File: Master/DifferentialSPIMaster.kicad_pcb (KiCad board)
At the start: 4 copper layers, 55.9 x 61 mm, 37 parts, among them J1 Motor Encoder 0, J2 Conn_01x20, J3 Motor Encoder 0, U1 MAX485E, U2 MAX485E, U3 MAX485E, U4 MAX485E, U5 MAX485E, U6 MAX485E

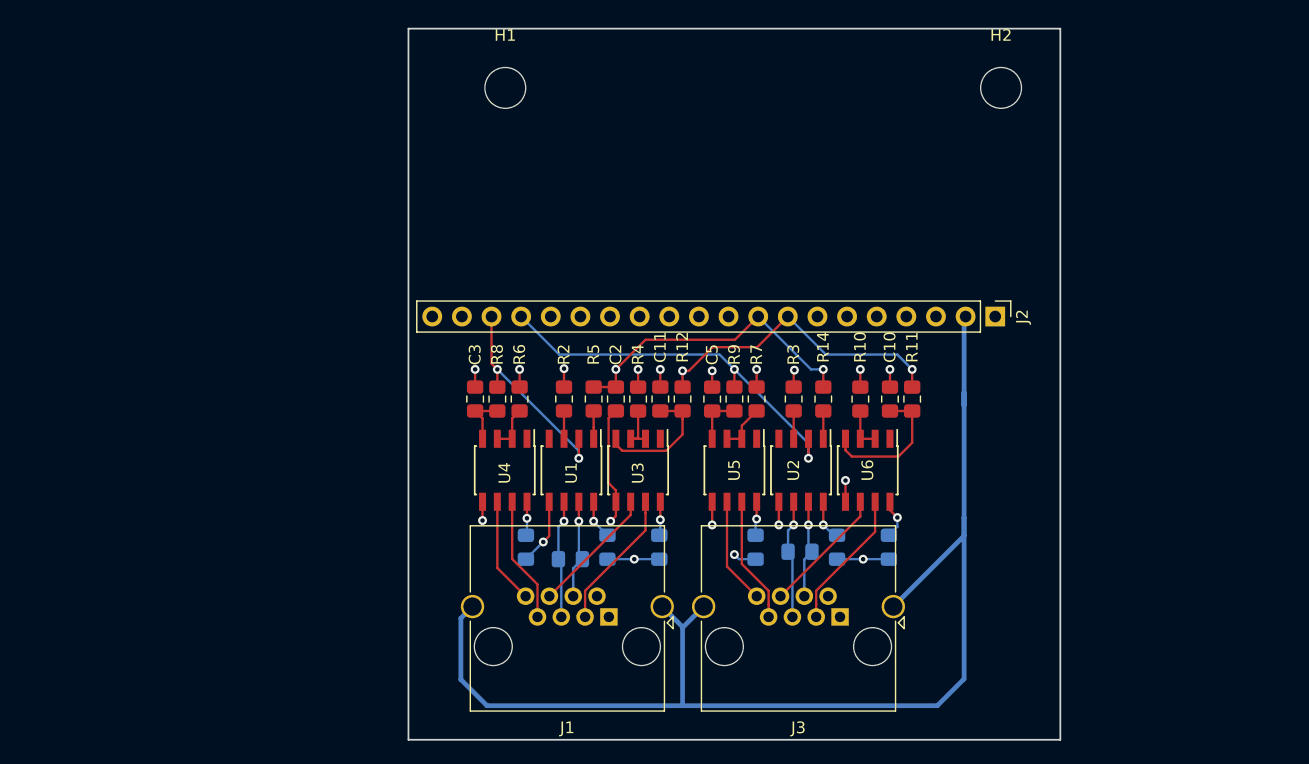
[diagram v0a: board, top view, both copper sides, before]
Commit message: Move board edge closer to RJ45s
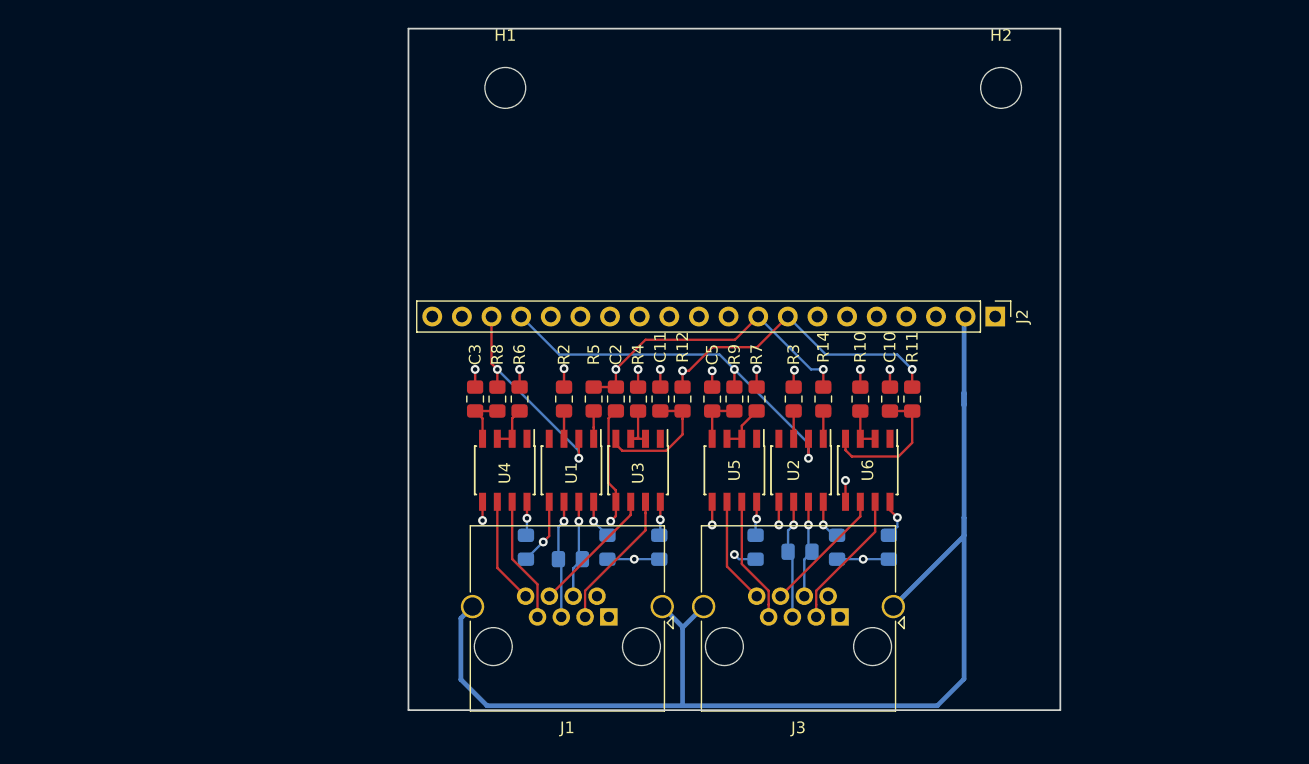
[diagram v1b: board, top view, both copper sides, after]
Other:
- board size 55.9 x 61 mm -> 55.9 x 58.4 mm
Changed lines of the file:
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@@
     )
   )
-  (gr_line (start 149.725 125.815) (end 93.845 125.815) (layer Edge.Cuts) (width 0.15))
-  (gr_line (start 149.725 64.855) (end 149.725 125.815) (layer Edge.Cuts) (width 0.15))
+  (gr_line (start 149.725 123.275) (end 93.845 123.275) (layer Edge.Cuts) (width 0.15))
+  (gr_line (start 149.725 64.855) (end 149.725 123.275) (layer Edge.Cuts) (width 0.15))
   (gr_line (start 93.845 64.855) (end 149.725 64.855) (layer Edge.Cuts) (width 0.15))
-  (gr_line (start 93.845 125.815) (end 93.845 64.855) (layer Edge.Cuts) (width 0.15))
+  (gr_line (start 93.845 123.275) (end 93.845 64.855) (layer Edge.Cuts) (width 0.15))
   (via (at 105.402 108.8605) (size 0.762) (drill 0.381) (layers F.Cu B.Cu) (net 1))
   (segment (start 103.915 110.335) (end 105.3895 108.8605) (width 0.2032) (layer B.Cu) (net 1))
@@
     (polygon
       (pts
-        (xy 93.845 87.715) (xy 149.725 87.715) (xy 149.725 125.815) (xy 93.845 125.815)
+        (xy 93.845 87.715) (xy 149.725 87.715) (xy 149.725 123.275) (xy 93.845 123.275)
       )
     )
@@
     (polygon
       (pts
-        (xy 93.845 87.715) (xy 149.725 87.715) (xy 149.725 125.815) (xy 93.845 125.815)
+        (xy 93.845 87.715) (xy 149.725 87.715) (xy 149.725 123.275) (xy 93.845 123.275)
       )
     )

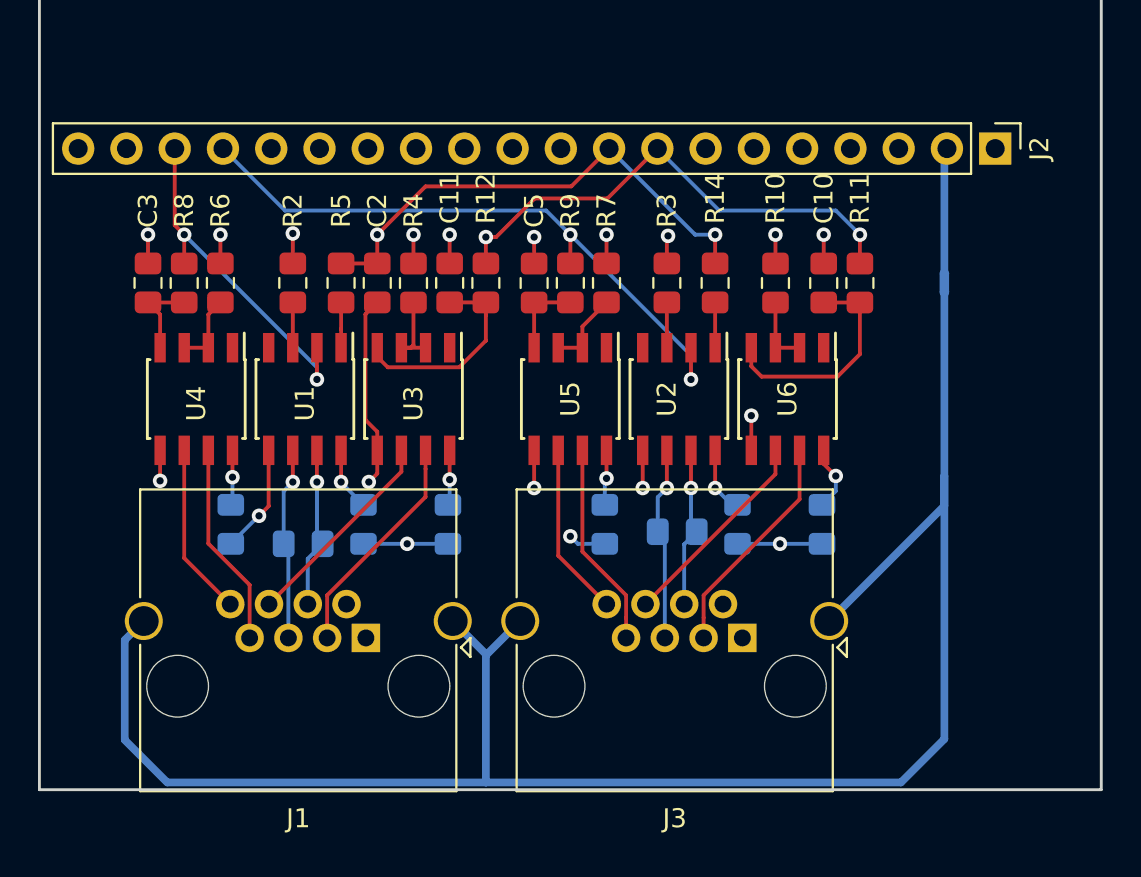
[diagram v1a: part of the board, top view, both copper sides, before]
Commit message: Add top/bottom fills, make board 2 layer
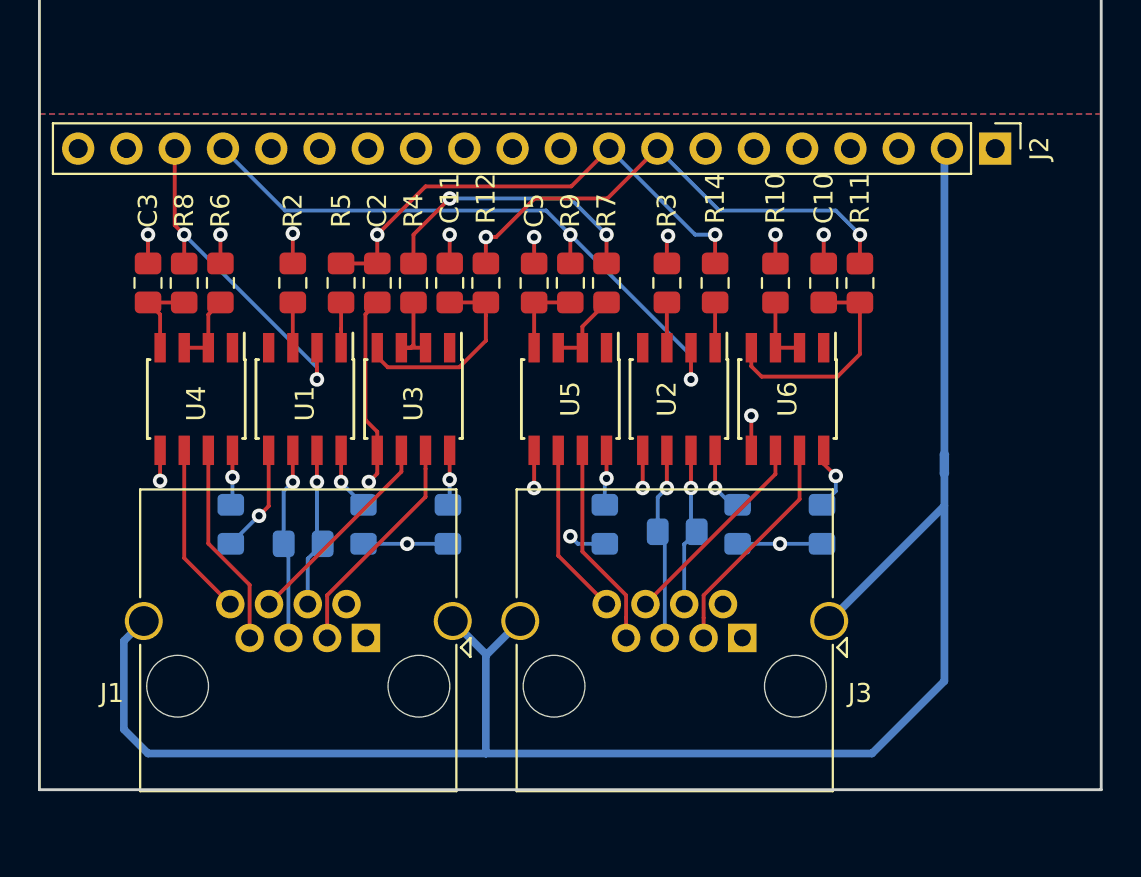
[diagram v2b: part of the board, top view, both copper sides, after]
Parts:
- moved NT1 9.52 mm to (141.5, 106.1)
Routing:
- net GND: track 97.1 -> 81.2 mm
- net +5V: track 25.1 -> 36.9 mm
- net GNDD: track 49.8 -> 59.3 mm
- added copper zone on F.Cu, net +5V
- added copper zone on B.Cu, net GNDD
- removed copper zone on In2.Cu, net +5V
- removed copper zone on In1.Cu, net GNDD
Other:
- copper layers 4 -> 2
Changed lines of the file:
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@@
     (thickness 1.6)
     (drawings 4)
-    (tracks 213)
+    (tracks 215)
     (zones 0)
     (modules 37)
@@
   (layers
     (0 F.Cu signal)
-    (1 In1.Cu signal)
-    (2 In2.Cu signal)
     (31 B.Cu signal)
     (32 B.Adhes user)
@@
     (46 B.CrtYd user)
     (47 F.CrtYd user)
-    (48 B.Fab user hide)
-    (49 F.Fab user hide)
+    (48 B.Fab user)
+    (49 F.Fab user)
   )
   (setup
@@
   )
   (module NetTie:NetTie-2_SMD_Pad0.5mm (layer B.Cu)
-    (at 141.47 96.605 90)
+    (at 141.47 106.13 90)
     (descr "Net tie, 2 pin, 0.5mm square SMD pads")
     (tags "net tie")
@@
     (descr "Shielded, https://www.amphenolcanada.com/ProductSearch/drawings/AC/RJHSE538X.pdf")
     (tags "RJ45 8p8c ethernet cat5")
-    (fp_text reference J3 (at 3.56 -9.5 180) (layer F.SilkS)
+    (fp_text reference J3 (at -6.186 -2.907 180) (layer F.SilkS)
       (effects (font (size 1 1) (thickness 0.15)))
     )
@@
     (descr "Shielded, https://www.amphenolcanada.com/ProductSearch/drawings/AC/RJHSE538X.pdf")
     (tags "RJ45 8p8c ethernet cat5")
-    (fp_text reference J1 (at 3.56 -9.5 180) (layer F.SilkS)
+    (fp_text reference J1 (at 13.372 -2.907 180) (layer F.SilkS)
       (effects (font (size 1 1) (thickness 0.15)))
     )
@@
   (segment (start 135.12 95.585) (end 135.12 94.065) (width 0.2032) (layer F.Cu) (net 1))
   (segment (start 141.47 89.67) (end 141.605 89.535) (width 0.4064) (layer B.Cu) (net 1))
-  (segment (start 141.47 96.105) (end 141.47 89.67) (width 0.4064) (layer B.Cu) (net 1))
+  (segment (start 141.47 105.63) (end 141.47 89.67) (width 0.4064) (layer B.Cu) (net 1))
   (segment (start 114.165 106.3932) (end 114.165 105.415) (width 0.2032) (layer F.Cu) (net 2))
   (segment (start 114.165 107.864078) (end 114.165 106.3932) (width 0.2032) (layer F.Cu) (net 2))
@@
   (segment (start 101.465 111.086) (end 103.887 113.508) (width 0.2032) (layer F.Cu) (net 7))
   (segment (start 101.465 105.415) (end 101.465 111.086) (width 0.2032) (layer F.Cu) (net 7))
-  (segment (start 98.337001 115.397999) (end 98.337001 120.655001) (width 0.4064) (layer B.Cu) (net 8))
-  (segment (start 99.337 114.398) (end 98.337001 115.397999) (width 0.4064) (layer B.Cu) (net 8))
-  (segment (start 98.337001 120.655001) (end 100.576 122.894) (width 0.4064) (layer B.Cu) (net 8))
   (segment (start 119.149 114.398) (end 117.34 116.207) (width 0.4064) (layer B.Cu) (net 8))
-  (segment (start 115.597 114.398) (end 117.34 116.141) (width 0.4064) (layer B.Cu) (net 8))
-  (segment (start 117.34 116.141) (end 117.34 122.894) (width 0.4064) (layer B.Cu) (net 8))
-  (segment (start 100.576 122.894) (end 117.34 122.894) (width 0.4064) (layer B.Cu) (net 8))
-  (segment (start 117.34 122.894) (end 139.184 122.894) (width 0.4064) (layer B.Cu) (net 8))
-  (segment (start 139.184 122.894) (end 141.47 120.608) (width 0.4064) (layer B.Cu) (net 8))
-  (segment (start 141.47 108.337) (end 141.47 106.765) (width 0.4064) (layer B.Cu) (net 8))
+  (segment (start 117.34 116.141) (end 115.597 114.398) (width 0.4064) (layer B.Cu) (net 8))
+  (segment (start 117.34 121.37) (end 117.34 116.141) (width 0.4064) (layer B.Cu) (net 8))
+  (segment (start 99.56 121.37) (end 117.34 121.37) (width 0.4064) (layer B.Cu) (net 8))
+  (segment (start 98.29 120.1) (end 99.56 121.37) (width 0.4064) (layer B.Cu) (net 8))
+  (segment (start 99.337 114.398) (end 98.29 115.445) (width 0.4064) (layer B.Cu) (net 8))
+  (segment (start 98.29 115.445) (end 98.29 120.1) (width 0.4064) (layer B.Cu) (net 8))
+  (segment (start 137.66 121.37) (end 117.34 121.37) (width 0.4064) (layer B.Cu) (net 8))
+  (segment (start 141.47 117.56) (end 137.66 121.37) (width 0.4064) (layer B.Cu) (net 8))
   (segment (start 135.409 114.398) (end 141.47 108.337) (width 0.4064) (layer B.Cu) (net 8))
-  (segment (start 141.47 120.608) (end 141.47 106.765) (width 0.4064) (layer B.Cu) (net 8))
-  (segment (start 141.47 106.765) (end 141.47 97.105) (width 0.4064) (layer B.Cu) (net 8))
+  (segment (start 141.47 108.337) (end 141.47 117.56) (width 0.4064) (layer B.Cu) (net 8))
+  (segment (start 141.47 108.337) (end 141.47 106.63) (width 0.4064) (layer B.Cu) (net 8))
   (segment (start 107.18 100.015) (end 107.18 97.63) (width 0.2032) (layer F.Cu) (net 20))
   (segment (start 114.165 100.015) (end 112.895 100.015) (width 0.2032) (layer F.Cu) (net 21))
@@
   (via (at 103.37 94.065) (size 0.762) (drill 0.381) (layers F.Cu B.Cu) (net 46))
   (segment (start 103.37 95.58) (end 103.37 94.065) (width 0.2032) (layer F.Cu) (net 46))
-  (via (at 113.53 94.065) (size 0.762) (drill 0.381) (layers F.Cu B.Cu) (net 46))
-  (segment (start 113.53 95.585) (end 113.53 94.065) (width 0.2032) (layer F.Cu) (net 46))
   (via (at 123.69 106.892) (size 0.762) (drill 0.381) (layers F.Cu B.Cu) (net 46))
   (segment (start 123.6 108.285) (end 123.6 106.982) (width 0.2032) (layer B.Cu) (net 46))
@@
   (via (at 132.58 94.065) (size 0.762) (drill 0.381) (layers F.Cu B.Cu) (net 46))
   (segment (start 132.58 95.585) (end 132.58 94.065) (width 0.2032) (layer F.Cu) (net 46))
-  (zone (net 46) (net_name +5V) (layer In2.Cu) (hatch edge 0.508)
+  (segment (start 123.69 94.065) (end 121.785 92.16) (width 0.2032) (layer B.Cu) (net 46))
+  (via (at 115.435 92.16) (size 0.762) (drill 0.381) (layers F.Cu B.Cu) (net 46))
+  (segment (start 121.785 92.16) (end 115.435 92.16) (width 0.2032) (layer B.Cu) (net 46))
+  (segment (start 113.53 94.065) (end 113.53 95.585) (width 0.2032) (layer F.Cu) (net 46))
+  (segment (start 115.435 92.16) (end 113.53 94.065) (width 0.2032) (layer F.Cu) (net 46))
+  (zone (net 46) (net_name +5V) (layer F.Cu) (hatch edge 0.508)
     (connect_pads (clearance 0.508))
     (min_thickness 0.254)
-    (fill yes (arc_segments 16) (thermal_gap 0.508) (thermal_bridge_width 0.508))
+    (fill yes (arc_segments 32) (thermal_gap 0.508) (thermal_bridge_width 0.508))
     (polygon
       (pts
@@
     )
   )
-  (zone (net 1) (net_name GNDD) (layer In1.Cu) (hatch edge 0.508)
+  (zone (net 1) (net_name GNDD) (layer B.Cu) (hatch edge 0.508)
     (connect_pads (clearance 0.508))
     (min_thickness 0.254)
-    (fill yes (arc_segments 16) (thermal_gap 0.508) (thermal_bridge_width 0.508))
+    (fill yes (arc_segments 32) (thermal_gap 0.508) (thermal_bridge_width 0.508))
     (polygon
       (pts

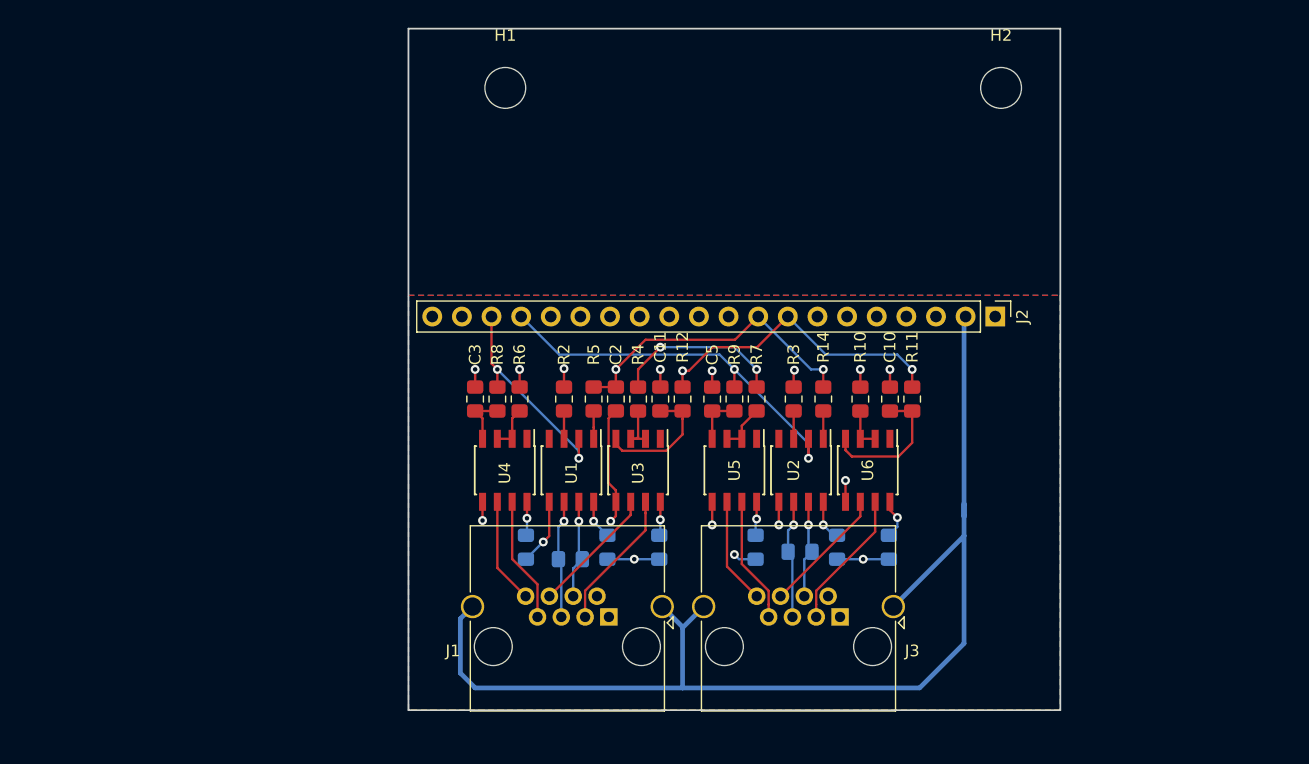
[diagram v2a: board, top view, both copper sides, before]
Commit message: Add pullups for CS lines and remove extra material from master
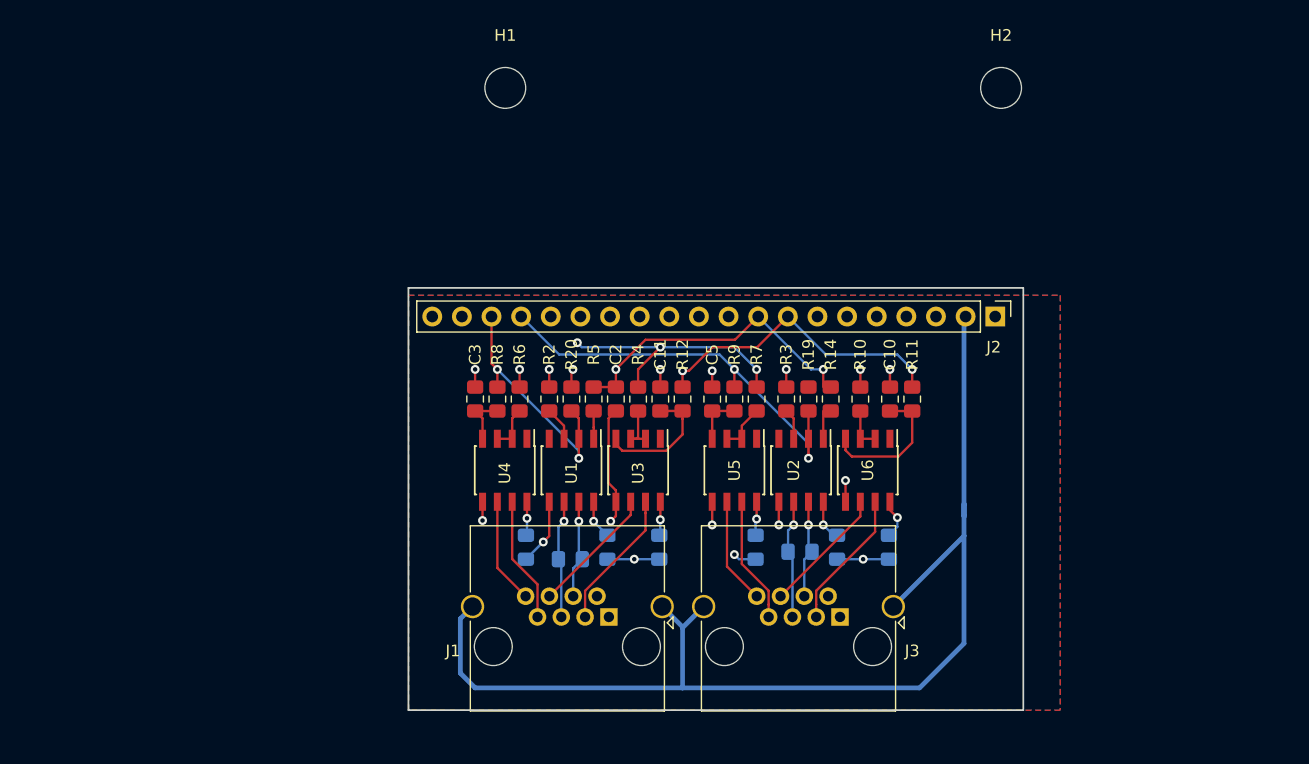
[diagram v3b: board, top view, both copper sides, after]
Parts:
- added R19: 10k, Resistor_SMD:R_0805_2012Metric_Pad1.15x1.40mm_HandSolder, F.Cu at (128.1, 96.6)
- added R20: 10k, Resistor_SMD:R_0805_2012Metric_Pad1.15x1.40mm_HandSolder, F.Cu at (107.8, 96.6)
- C10, C11, C2, C3, C5: value 100nF -> 2.2pF
- R11, R12, R14, R5, R8, R9: value R -> 1k
- U1, U2, U3, U4, U5, U6: value MAX485E -> SN65HVD06D
- moved R2 1.27 mm to (105.9, 96.6)
- moved R14 0.63 mm to (130.0, 96.6)
- moved R3 0.63 mm to (126.2, 96.6)
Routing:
- net +5V: track 36.9 -> 45.7 mm, vias 10 -> 12
- net /CS_1: track 18.4 -> 21.1 mm
- net /CS_2: track 33.6 -> 36.0 mm
- net Net-(R2-Pad1): track 2.39 -> 2.91 mm
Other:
- board size 55.9 x 58.4 mm -> 52.7 x 36.2 mm
